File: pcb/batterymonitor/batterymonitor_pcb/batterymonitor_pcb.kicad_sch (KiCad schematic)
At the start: 9 parts, among them J1 12V_Input, J2 Conn_01x04_Pin, U1 AMS1117-3.3, U2 ESP32-WROOM-32U-N4

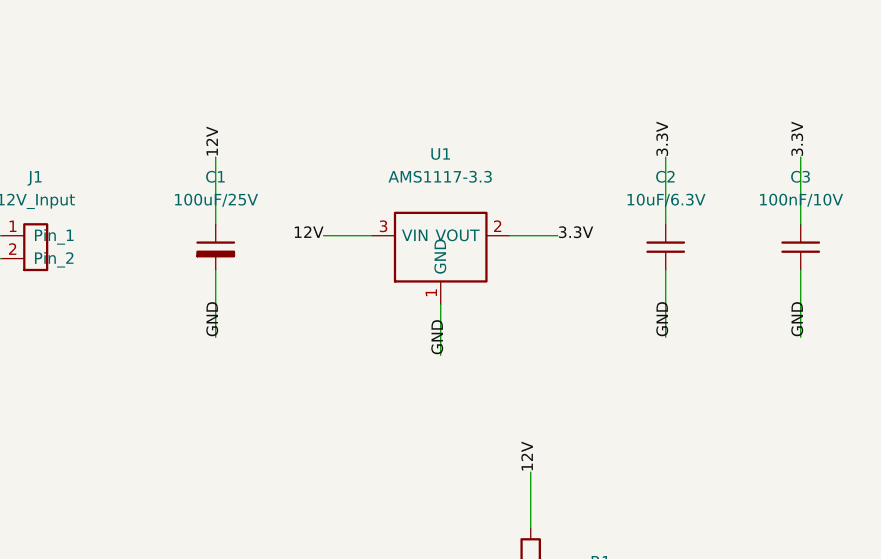
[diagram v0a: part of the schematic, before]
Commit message: Implement AP63300 buck converter design in PCB and schematic
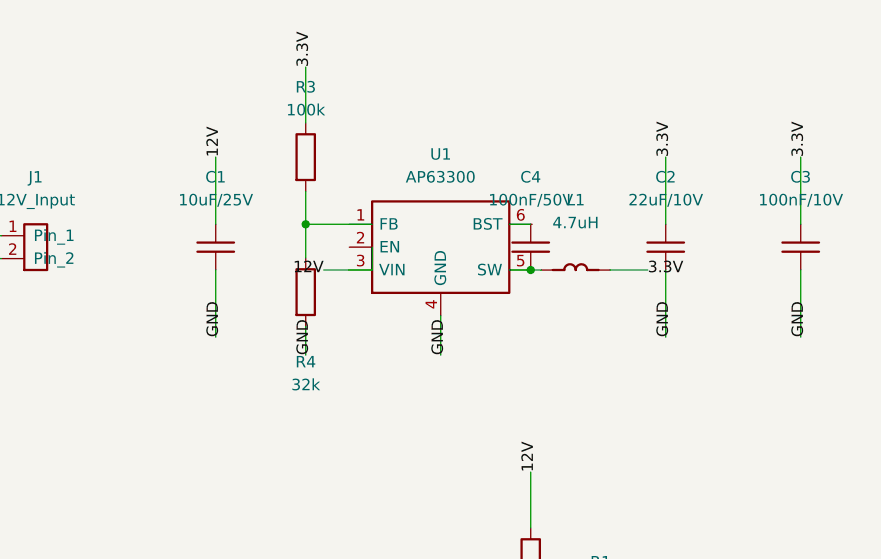
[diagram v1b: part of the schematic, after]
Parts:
- added C4: 100nF/50V, Capacitor_SMD:C_0805_2012Metric, symbol Device:C
- added L1: 4.7uH, Inductor_SMD:L_0806_2012Metric, symbol Device:L
- added R3: 100k, Resistor_SMD:R_0805_2012Metric, symbol Device:R
- added R4: 32k, Resistor_SMD:R_0805_2012Metric, symbol Device:R
- C1: value 100uF/25V -> 10uF/25V; footprint Capacitor_SMD:CP_Elec_6.3x5.4 -> Capacitor_SMD:C_0805_2012Metric; symbol Device:C_Polarized -> Device:C; LCSC C162594 -> C40894
- C2: value 10uF/6.3V -> 22uF/10V; LCSC C15849 -> C89572
- U1: value AMS1117-3.3 -> AP63300; footprint Package_TO_SOT_SMD:SOT-223-3_TabPin2 -> Package_TO_SOT_SMD:TSOT-23-6; symbol Regulator_Linear:AMS1117-3.3 -> Regulator_Switching:AP63300; LCSC C6186 -> C2158012
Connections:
- net 12V: no longer U1.3 (VIN)
- net 3.3V: now also L1.2, R3.1; no longer U1.2 (VOUT)
- net GND: now also U1.4 (GND), R4.2; no longer U1.1 (GND)
- new net: C4.2, L1.1
- new net: R3.2, R4.1
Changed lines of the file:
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@@
     (pin "2")
   )
-  (symbol (lib_id "Device:C_Polarized") (at 60 70 0) (unit 1)
+  (symbol (lib_id "Device:C") (at 60 70 0) (unit 1)
     (property "Reference" "C1" (at 60 62.23 0) (effects (font (size 1.27 1.27))))
-    (property "Value" "100uF/25V" (at 60 64.77 0) (effects (font (size 1.27 1.27))))
-    (property "Footprint" "Capacitor_SMD:CP_Elec_6.3x5.4" (at 60 70 0) (effects (font (size 1.27 1.27)) hide))
-    (property "LCSC" "C162594" (at 60 70 0) (effects (font (size 1.27 1.27)) hide))
+    (property "Value" "10uF/25V" (at 60 64.77 0) (effects (font (size 1.27 1.27))))
+    (property "Footprint" "Capacitor_SMD:C_0805_2012Metric" (at 60 70 0) (effects (font (size 1.27 1.27)) hide))
+    (property "LCSC" "C40894" (at 60 70 0) (effects (font (size 1.27 1.27)) hide))
     (pin "1")
     (pin "2")
   )
-  (symbol (lib_id "Regulator_Linear:AMS1117-3.3") (at 85 70 0) (unit 1)
+  (symbol (lib_id "Regulator_Switching:AP63300") (at 85 70 0) (unit 1)
     (property "Reference" "U1" (at 85 59.69 0) (effects (font (size 1.27 1.27))))
-    (property "Value" "AMS1117-3.3" (at 85 62.23 0) (effects (font (size 1.27 1.27))))
-    (property "Footprint" "Package_TO_SOT_SMD:SOT-223-3_TabPin2" (at 85 70 0) (effects (font (size 1.27 1.27)) hide))
-    (property "LCSC" "C6186" (at 85 70 0) (effects (font (size 1.27 1.27)) hide))
+    (property "Value" "AP63300" (at 85 62.23 0) (effects (font (size 1.27 1.27))))
+    (property "Footprint" "Package_TO_SOT_SMD:TSOT-23-6" (at 85 70 0) (effects (font (size 1.27 1.27)) hide))
+    (property "LCSC" "C2158012" (at 85 70 0) (effects (font (size 1.27 1.27)) hide))
     (pin "1")
     (pin "2")
     (pin "3")
+    (pin "4")
+    (pin "5")
+    (pin "6")
   )
   (symbol (lib_id "Device:C") (at 110 70 0) (unit 1)
     (property "Reference" "C2" (at 110 62.23 0) (effects (font (size 1.27 1.27))))
-    (property "Value" "10uF/6.3V" (at 110 64.77 0) (effects (font (size 1.27 1.27))))
+    (property "Value" "22uF/10V" (at 110 64.77 0) (effects (font (size 1.27 1.27))))
     (property "Footprint" "Capacitor_SMD:C_0805_2012Metric" (at 110 70 0) (effects (font (size 1.27 1.27)) hide))
-    (property "LCSC" "C15849" (at 110 70 0) (effects (font (size 1.27 1.27)) hide))
+    (property "LCSC" "C89572" (at 110 70 0) (effects (font (size 1.27 1.27)) hide))
+    (pin "1")
+    (pin "2")
+  )
+  (symbol (lib_id "Device:L") (at 100 72.54 0) (unit 1)
+    (property "Reference" "L1" (at 100 64.77 0) (effects (font (size 1.27 1.27))))
+    (property "Value" "4.7uH" (at 100 67.31 0) (effects (font (size 1.27 1.27))))
+    (property "Footprint" "Inductor_SMD:L_0806_2012Metric" (at 100 72.54 0) (effects (font (size 1.27 1.27)) hide))
+    (property "LCSC" "C98335" (at 100 72.54 0) (effects (font (size 1.27 1.27)) hide))
+    (pin "1")
+    (pin "2")
+  )
+  (symbol (lib_id "Device:C") (at 95 70 0) (unit 1)
+    (property "Reference" "C4" (at 95 62.23 0) (effects (font (size 1.27 1.27))))
+    (property "Value" "100nF/50V" (at 95 64.77 0) (effects (font (size 1.27 1.27))))
+    (property "Footprint" "Capacitor_SMD:C_0805_2012Metric" (at 95 70 0) (effects (font (size 1.27 1.27)) hide))
+    (property "LCSC" "C49678" (at 95 70 0) (effects (font (size 1.27 1.27)) hide))
+    (pin "1")
+    (pin "2")
+  )
+  (symbol (lib_id "Device:R") (at 70 60 0) (unit 1)
+    (property "Reference" "R3" (at 70 52.23 0) (effects (font (size 1.27 1.27))))
+    (property "Value" "100k" (at 70 54.77 0) (effects (font (size 1.27 1.27))))
+    (property "Footprint" "Resistor_SMD:R_0805_2012Metric" (at 70 60 0) (effects (font (size 1.27 1.27)) hide))
+    (property "LCSC" "C149504" (at 70 60 0) (effects (font (size 1.27 1.27)) hide))
+    (pin "1")
+    (pin "2")
+  )
+  (symbol (lib_id "Device:R") (at 70 75 0) (unit 1)
+    (property "Reference" "R4" (at 70 82.77 0) (effects (font (size 1.27 1.27))))
+    (property "Value" "32k" (at 70 85.31 0) (effects (font (size 1.27 1.27))))
+    (property "Footprint" "Resistor_SMD:R_0805_2012Metric" (at 70 75 0) (effects (font (size 1.27 1.27)) hide))
+    (property "LCSC" "C182555" (at 70 75 0) (effects (font (size 1.27 1.27)) hide))
     (pin "1")
     (pin "2")
@@
   (wire (pts (xy 60 72.54) (xy 60 80)))
   (label "GND" (at 60 80 270) (effects (font (size 1.27 1.27)) (justify left)))
-  (wire (pts (xy 77.38 68.73) (xy 72 68.73)))
-  (label "12V" (at 72 68.73 180) (effects (font (size 1.27 1.27)) (justify right)))
-  (wire (pts (xy 92.62 68.73) (xy 98 68.73)))
-  (label "3.3V" (at 98 68.73 0) (effects (font (size 1.27 1.27)) (justify left)))
-  (wire (pts (xy 85 76.35) (xy 85 82)))
+  (wire (pts (xy 77.38 70) (xy 77.38 72.54)))
+  (wire (pts (xy 77.38 72.54) (xy 72 72.54)))
+  (label "12V" (at 72 72.54 180) (effects (font (size 1.27 1.27)) (justify right)))
+  (wire (pts (xy 77.38 67.46) (xy 70 67.46)))
+  (junction (at 70 67.46) (diameter 0) (color 0 0 0 0))
+  (wire (pts (xy 70 67.46) (xy 70 63.81)))
+  (wire (pts (xy 70 67.46) (xy 70 71.19)))
+  (wire (pts (xy 70 56.19) (xy 70 50)))
+  (label "3.3V" (at 70 50 90) (effects (font (size 1.27 1.27)) (justify left)))
+  (wire (pts (xy 70 78.81) (xy 70 82)))
+  (label "GND" (at 70 82 270) (effects (font (size 1.27 1.27)) (justify left)))
+  (wire (pts (xy 85 77.62) (xy 85 82)))
   (label "GND" (at 85 82 270) (effects (font (size 1.27 1.27)) (justify left)))
+  (wire (pts (xy 92.62 67.46) (xy 95 67.46)))
+  (wire (pts (xy 92.62 72.54) (xy 95 72.54)))
+  (junction (at 95 72.54) (diameter 0) (color 0 0 0 0))
+  (wire (pts (xy 95 72.54) (xy 96.19 72.54)))
+  (wire (pts (xy 103.81 72.54) (xy 108 72.54)))
+  (label "3.3V" (at 108 72.54 0) (effects (font (size 1.27 1.27)) (justify left)))
   (wire (pts (xy 110 67.46) (xy 110 60)))
   (label "3.3V" (at 110 60 90) (effects (font (size 1.27 1.27)) (justify left)))

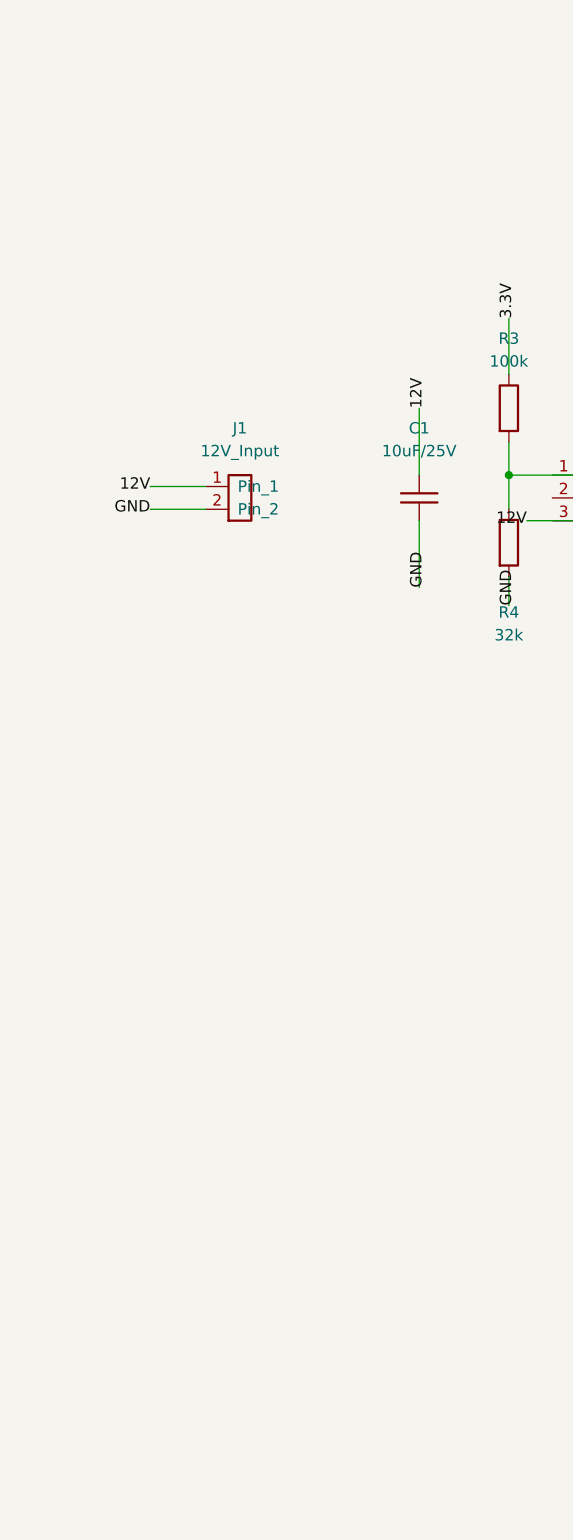
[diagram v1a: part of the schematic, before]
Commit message: Add DC Jack Female component to BOM files for battery monitor PCB
- Added DC Jack Female (J4) to both bom_jlcpcb.csv and bom_pcbway.csv
- Updated component details including footprint and manufacturer information
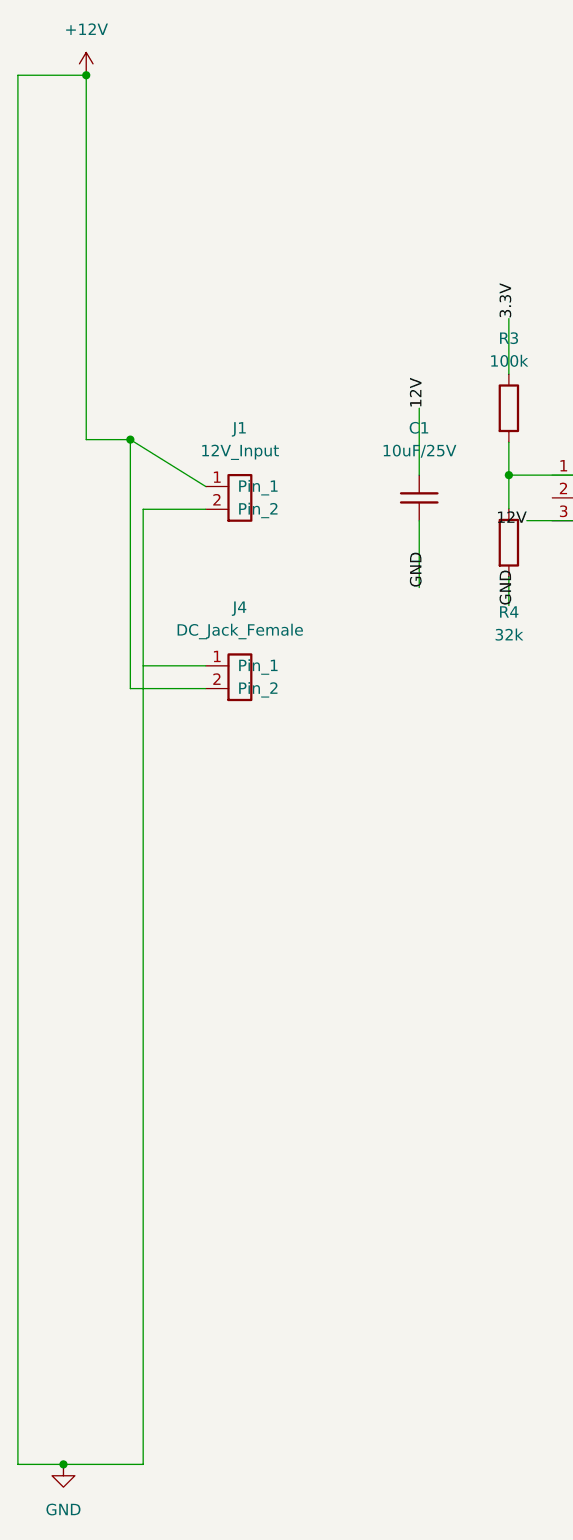
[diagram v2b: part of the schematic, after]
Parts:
- added J4: DC_Jack_Female, Connector_BarrelJack:BarrelJack_Horizontal, symbol Connector:Conn_01x02_Pin
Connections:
- net 12V: no longer J1.1 (Pin_1)
- net GND renamed +12V
- net +12V: now also J1.1 (Pin_1), J4.2 (Pin_2)
